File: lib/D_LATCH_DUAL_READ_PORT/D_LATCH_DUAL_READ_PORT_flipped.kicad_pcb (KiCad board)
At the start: 2 copper layers, 18 parts

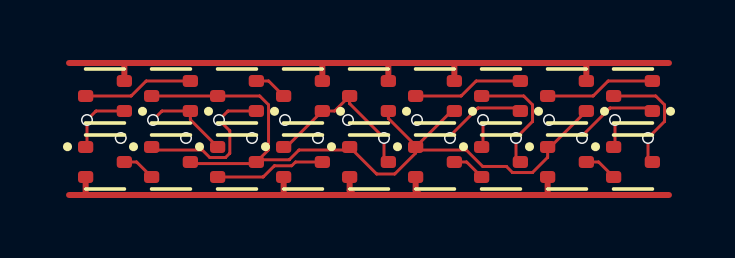
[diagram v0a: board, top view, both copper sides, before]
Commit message: All cells now use 1mm*4mm grid rather than 1.1mm*4.4mm
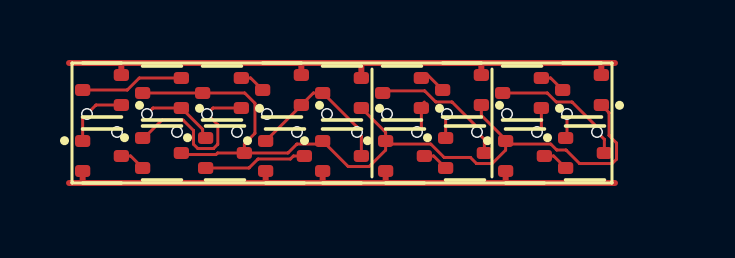
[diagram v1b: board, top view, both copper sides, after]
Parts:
- moved port2.N2 3.70 mm to (15.0, 1.00)
- moved port1.N2 3.30 mm to (11.0, 1.00)
- moved port2.P2 1.63 mm to (17.1, 3.00)
- moved port2.P1 1.41 mm to (15.1, 3.10)
- moved port1.P2 1.24 mm to (13.1, 3.00)
- moved port1.P1 1.02 mm to (11.1, 3.10)
- moved port1.N1 0.92 mm to (13.0, 0.90)
- moved latch.NOT2.P1 0.92 mm to (9.00, 3.10)
- moved latch.NOT2.N1 0.91 mm to (9.00, 1.00)
- moved latch.NOT3.N1 0.73 mm to (7.00, 0.90)
- moved latch.NOT3.P1 0.63 mm to (7.10, 3.10)
- moved port2.N1 0.54 mm to (17.0, 0.90)
- moved latch.NOT3.N2 0.51 mm to (5.00, 1.00)
- moved latch.NOT3.P2 0.50 mm to (5.10, 3.00)
- moved latch.NOT1.P2 0.42 mm to (3.00, 3.00)
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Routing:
- net VDD: track 23.2 -> 20.3 mm
- net port2.intN: track 3.70 -> 0.88 mm
- net port1.intN: track 3.70 -> 0.92 mm
- net GND: track 23.1 -> 20.3 mm
- net latch.NOT1.Y: track 25.2 -> 27.4 mm
- net EN2: track 2.84 -> 0.86 mm
- net EN1: track 2.84 -> 1.07 mm
- net Q1: track 4.01 -> 4.61 mm
- net Q2: track 4.01 -> 4.58 mm

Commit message: Make the pads of my SOT523 footprint very slightly smaller, which is enough to route all the cells and leave the mosfets exactly on the grid
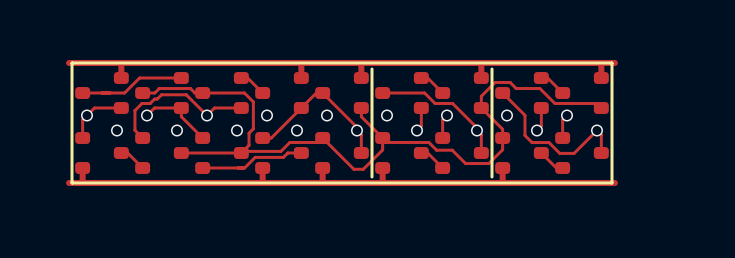
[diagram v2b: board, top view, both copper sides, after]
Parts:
- latch.NOT1.N1, latch.NOT1.N2, latch.NOT1.P1, latch.NOT1.P2, latch.NOT2.N1, latch.NOT2.P1, latch.NOT3.N1, latch.NOT3.N2, latch.NOT3.P1, latch.NOT3.P2, port1.N1, port1.N2, port1.P1, port1.P2, port2.N1, port2.N2, port2.P1, port2.P2: footprint Package_TO_SOT_SMD:SOT-523 -> RV523:SOT523
- moved latch.NOT3.P1 0.14 mm to (7.00, 3.00)
- moved port1.P1 0.14 mm to (11.0, 3.00)
- moved port2.P1 0.14 mm to (15.0, 3.00)
- moved port2.P2 0.10 mm to (17.0, 3.00)
- moved latch.NOT1.P1 0.10 mm to (1.00, 3.00)
- moved latch.NOT2.P1 0.10 mm to (9.00, 3.00)
- moved latch.NOT1.N1 0.10 mm to (1.00, 1.00)
- moved latch.NOT3.N1 0.10 mm to (7.00, 1.00)
- moved port1.N1 0.10 mm to (13.0, 1.00)
- moved port2.N1 0.10 mm to (17.0, 1.00)
- moved latch.NOT3.P2 0.10 mm to (5.00, 3.00)
- moved port1.P2 0.10 mm to (13.0, 3.00)
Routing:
- net latch.NOT1.Y: track 27.4 -> 26.3 mm
- net Q2: track 4.58 -> 5.50 mm
- net nCLK: track 5.86 -> 5.17 mm

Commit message: Propagate MOSFET values to the cells' PCBs
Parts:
- latch.NOT1.N1, latch.NOT1.N2, latch.NOT2.N1, latch.NOT3.N1, latch.NOT3.N2, port1.N1, port1.N2, port2.N1, port2.N2: value (none) -> NMOS
- latch.NOT1.P1, latch.NOT1.P2, latch.NOT2.P1, latch.NOT3.P1, latch.NOT3.P2, port1.P1, port1.P2, port2.P1, port2.P2: value (none) -> PMOS
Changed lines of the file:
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@@
 			)
 		)
-		(property "Value" ""
+		(property "Value" "NMOS"
 			(at 0 0 180)
 			(layer "F.Fab")
@@
 			)
 		)
-		(property "Value" ""
+		(property "Value" "PMOS"
 			(at 0 0 0)
 			(layer "F.Fab")
@@
 			)
 		)
-		(property "Value" ""
+		(property "Value" "NMOS"
 			(at 0 0 180)
 			(layer "F.Fab")
@@
 			)
 		)
-		(property "Value" ""
+		(property "Value" "PMOS"
 			(at 0 0 0)
 			(layer "F.Fab")
@@
 			)
 		)
-		(property "Value" ""
+		(property "Value" "PMOS"
 			(at 0 0 0)
 			(layer "F.Fab")
@@
 			)
 		)
-		(property "Value" ""
+		(property "Value" "NMOS"
 			(at 0 0 180)
 			(layer "F.Fab")
@@
 			)
 		)
-		(property "Value" ""
+		(property "Value" "NMOS"
 			(at 0 0 180)
 			(layer "F.Fab")
@@
 			)
 		)
-		(property "Value" ""
+		(property "Value" "NMOS"
 			(at 0 0 180)
 			(layer "F.Fab")
@@
 			)
 		)
-		(property "Value" ""
+		(property "Value" "PMOS"
 			(at 0 0 0)
 			(layer "F.Fab")
@@
 			)
 		)
-		(property "Value" ""
+		(property "Value" "PMOS"
 			(at 0 0 0)
 			(layer "F.Fab")
@@
 			)
 		)
-		(property "Value" ""
+		(property "Value" "NMOS"
 			(at 0 0 180)
 			(layer "F.Fab")
@@
 			)
 		)
-		(property "Value" ""
+		(property "Value" "PMOS"
 			(at 0 0 0)
 			(layer "F.Fab")
@@
 			)
 		)
-		(property "Value" ""
+		(property "Value" "PMOS"
 			(at 0 0 0)
 			(layer "F.Fab")
@@
 			)
 		)
-		(property "Value" ""
+		(property "Value" "NMOS"
 			(at 0 0 180)
 			(layer "F.Fab")
@@
 			)
 		)
-		(property "Value" ""
+		(property "Value" "PMOS"
 			(at 0 0 0)
 			(layer "F.Fab")
@@
 			)
 		)
-		(property "Value" ""
+		(property "Value" "PMOS"
 			(at 0 0 0)
 			(layer "F.Fab")
@@
 			)
 		)
-		(property "Value" ""
+		(property "Value" "NMOS"
 			(at 0 0 180)
 			(layer "F.Fab")
@@
 			)
 		)
-		(property "Value" ""
-			(at 0 0 180)
-			(layer "F.Fab")
+		(property "Value" "NMOS"
+			(at 0 0 180)
+			(layer "F.Fab")
